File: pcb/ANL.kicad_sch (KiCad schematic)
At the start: 70 parts, among them J1 Conn_01x10_Socket, J10 Conn_01x02_Socket, J11 Conn_01x02_Socket, J12 Conn_01x02_Socket, J13 Conn_01x02_Socket, J14 Conn_01x02_Socket, J15 Conn_01x02_Socket, J16 Conn_01x02_Socket, J17 Conn_01x02_Socket, J18 Conn_01x02_Socket, J19 Conn_01x02_Socket, J2 Conn_01x02_Pin, J20 Conn_01x02_Socket, J21 Conn_01x02_Socket, J22 Conn_01x02_Socket, J23 Conn_01x02_Socket, J24 Conn_01x02_Socket, J25 Conn_01x02_Socket, J26 Conn_01x02_Socket, J27 Conn_01x02_Socket, J28 Conn_01x02_Socket, J29 Conn_01x02_Socket, J3 Conn_01x10_Socket, J30 Conn_01x02_Socket, J31 Conn_01x02_Socket, J32 Conn_01x02_Socket, J33 Conn_01x02_Socket, J4 Conn_02x02_Counter_Clockwise, J5 Conn_02x02_Counter_Clockwise, J6 Conn_02x02_Counter_Clockwise, J7 Conn_02x02_Counter_Clockwise, J8 Conn_02x02_Counter_Clockwise, J9 Conn_02x02_Counter_Clockwise, U1 4081, U2 4081

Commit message: Add missing vendor
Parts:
- U1, U2: Vendor (none) -> DigiKey; VendorId (none) -> 296-14280-5-ND
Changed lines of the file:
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@@
+      (effects (font (size 1.27 1.27)) hide)
+    )
+    (property "Vendor" "DigiKey" (at 138.43 105.41 0)
+      (effects (font (size 1.27 1.27)) hide)
+    )
+    (property "VendorId" "296-14280-5-ND" (at 138.43 105.41 0)
       (effects (font (size 1.27 1.27)) hide)
     )
@@
     )
     (property "Datasheet" "http://www.intersil.com/content/dam/Intersil/documents/cd40/cd4073bms-81bms-82bms.pdf" (at 115.57 105.41 0)
+      (effects (font (size 1.27 1.27)) hide)
+    )
+    (property "Vendor" "DigiKey" (at 115.57 105.41 0)
+      (effects (font (size 1.27 1.27)) hide)
+    )
+    (property "VendorId" "296-14280-5-ND" (at 115.57 105.41 0)
       (effects (font (size 1.27 1.27)) hide)
     )
@@
       (effects (font (size 1.27 1.27)) hide)
     )
+    (property "Vendor" "DigiKey" (at 92.71 105.41 0)
+      (effects (font (size 1.27 1.27)) hide)
+    )
+    (property "VendorId" "296-14280-5-ND" (at 92.71 105.41 0)
+      (effects (font (size 1.27 1.27)) hide)
+    )
     (pin "14")
     (pin "1")
@@
       (effects (font (size 1.27 1.27)) hide)
     )
+    (property "Vendor" "DigiKey" (at 137.16 38.1 0)
+      (effects (font (size 1.27 1.27)) hide)
+    )
+    (property "VendorId" "296-14280-5-ND" (at 137.16 38.1 0)
+      (effects (font (size 1.27 1.27)) hide)
+    )
     (pin "8")
     (pin "12")
@@
     )
     (property "Datasheet" "http://www.intersil.com/content/dam/Intersil/documents/cd40/cd4073bms-81bms-82bms.pdf" (at 114.3 38.1 0)
+      (effects (font (size 1.27 1.27)) hide)
+    )
+    (property "Vendor" "DigiKey" (at 114.3 38.1 0)
+      (effects (font (size 1.27 1.27)) hide)
+    )
+    (property "VendorId" "296-14280-5-ND" (at 114.3 38.1 0)
       (effects (font (size 1.27 1.27)) hide)
     )
@@
       (effects (font (size 1.27 1.27)) hide)
     )
+    (property "Vendor" "DigiKey" (at 46.99 105.41 0)
+      (effects (font (size 1.27 1.27)) hide)
+    )
+    (property "VendorId" "296-14280-5-ND" (at 46.99 105.41 0)
+      (effects (font (size 1.27 1.27)) hide)
+    )
     (pin "14")
     (pin "1")
@@
       (effects (font (size 1.27 1.27)) hide)
     )
+    (property "Vendor" "DigiKey" (at 207.01 105.41 0)
+      (effects (font (size 1.27 1.27)) hide)
+    )
+    (property "VendorId" "296-14280-5-ND" (at 207.01 105.41 0)
+      (effects (font (size 1.27 1.27)) hide)
+    )
     (pin "8")
     (pin "12")
@@
     )
     (property "Datasheet" "http://www.intersil.com/content/dam/Intersil/documents/cd40/cd4073bms-81bms-82bms.pdf" (at 184.15 105.41 0)
+      (effects (font (size 1.27 1.27)) hide)
+    )
+    (property "Vendor" "DigiKey" (at 184.15 105.41 0)
+      (effects (font (size 1.27 1.27)) hide)
+    )
+    (property "VendorId" "296-14280-5-ND" (at 184.15 105.41 0)
       (effects (font (size 1.27 1.27)) hide)
     )
@@
     )
     (property "Datasheet" "http://www.intersil.com/content/dam/Intersil/documents/cd40/cd4073bms-81bms-82bms.pdf" (at 69.85 105.41 0)
+      (effects (font (size 1.27 1.27)) hide)
+    )
+    (property "Vendor" "DigiKey" (at 69.85 105.41 0)
+      (effects (font (size 1.27 1.27)) hide)
+    )
+    (property "VendorId" "296-14280-5-ND" (at 69.85 105.41 0)
       (effects (font (size 1.27 1.27)) hide)
     )
@@
       (effects (font (size 1.27 1.27)) hide)
     )
+    (property "Vendor" "DigiKey" (at 161.29 105.41 0)
+      (effects (font (size 1.27 1.27)) hide)
+    )
+    (property "VendorId" "296-14280-5-ND" (at 161.29 105.41 0)
+      (effects (font (size 1.27 1.27)) hide)
+    )

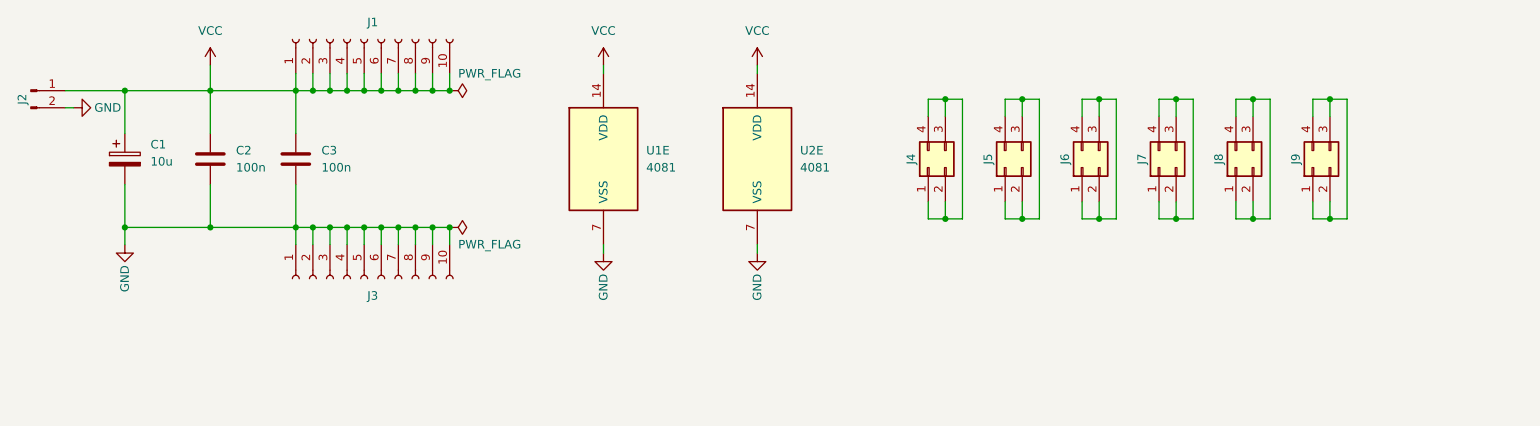
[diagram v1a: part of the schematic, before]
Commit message: Add reverse polarity protection
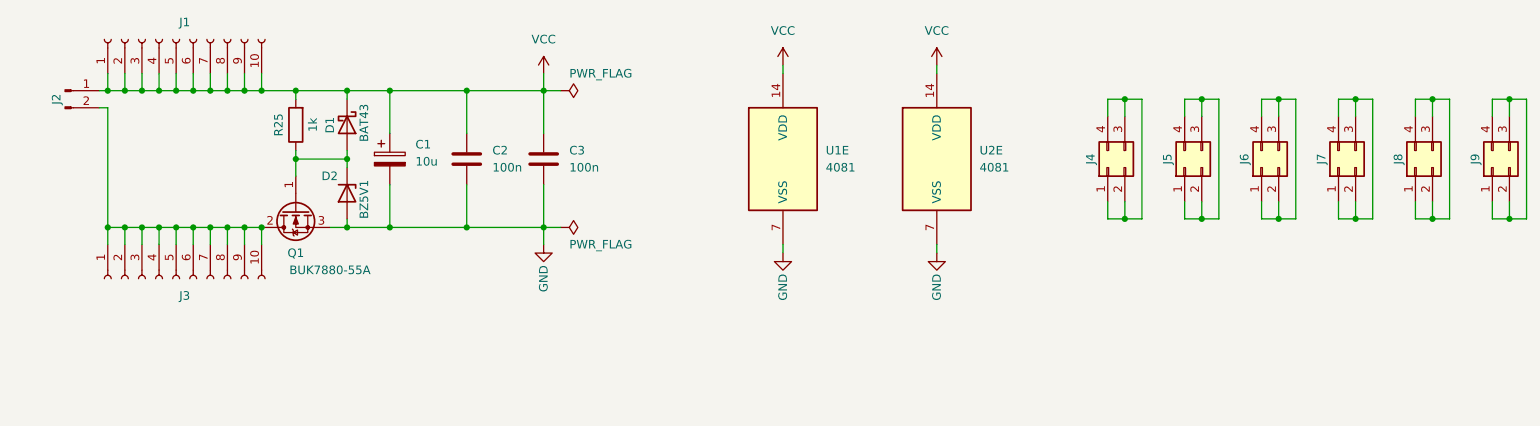
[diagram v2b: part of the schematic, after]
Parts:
- added D1: BAT43, Diode_SMD:D_MiniMELF, symbol Device:D_Schottky
- added D2: BZ5V1, Diode_SMD:D_MiniMELF, symbol Diode:BZV55B15
- added Q1: BUK7880-55A, Package_TO_SOT_SMD:SOT-223-3_TabPin2, symbol Transistor_FET:BUK7880-55A
- added R25: 1k, Resistor_SMD:R_1206_3216Metric, symbol Device:R
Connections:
- net GND: now also D2.2 (A), Q1.3 (S); no longer J2.2 (Pin_2), J3.1 (Pin_1), J3.10 (Pin_10), J3.2 (Pin_2), J3.3 (Pin_3), J3.4 (Pin_4), J3.5 (Pin_5), J3.6 (Pin_6), J3.7 (Pin_7), J3.8 (Pin_8), J3.9 (Pin_9)
- net VCC: now also D1.1 (K), R25.2
- new net: D1.2 (A), D2.1 (K), Q1.1 (G), R25.1
- new net: J2.2 (Pin_2), J3.1 (Pin_1), J3.10 (Pin_10), J3.2 (Pin_2), J3.3 (Pin_3), J3.4 (Pin_4), J3.5 (Pin_5), J3.6 (Pin_6), J3.7 (Pin_7), J3.8 (Pin_8), J3.9 (Pin_9), Q1.2 (D)
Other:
- moved on the sheet: C1, C2, C3, J1, J2, J3, J4, J5, J6, J7, J8, J9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
